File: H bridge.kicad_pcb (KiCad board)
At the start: 2 copper layers, 97 x 50 mm, 52 parts, among them J1 Fan, J2 5v Output, J3 Motor Terminal, J4 24v Power Input, J5 Control, J6 5v Output, J7 ICSP, Q1 IRLZ44N, Q2 IRLZ44N, Q3 IRLZ44N, Q4 IRLZ44N, SW1 SW_SPST, U1 IR2110, U2 IR2110, U3 LM7815_TO220, U4 ATmega328P-A, U5 LM7805_TO220, Y1 16MHz

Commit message: just made some modification for the final revision.. I might manufacture this one.
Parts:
- U3: value LM7815_TO220 -> LM7815
- U5: value LM7805_TO220 -> LM7805
- renumbered SW1 to OFF/ON

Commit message: small edit in pcb for fabrication.
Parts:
- added REF**: WEEE-Logo_5.6x8mm_SilkScreen, Symbol:WEEE-Logo_5.6x8mm_SilkScreen, B.Cu at (143.0, 104.5)
- added REF**: KiCad-Logo2_6mm_SilkScreen, Symbol:KiCad-Logo2_6mm_SilkScreen, B.Cu at (180.0, 91.0)
- added REF**: OSHW-Logo_7.5x8mm_SilkScreen, Symbol:OSHW-Logo_7.5x8mm_SilkScreen, B.Cu at (150.5, 104.5)
- moved G*** 0.79 mm to (174.0, 96.0)
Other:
- board text added: "v2.1"
- board text removed: "v2.0"

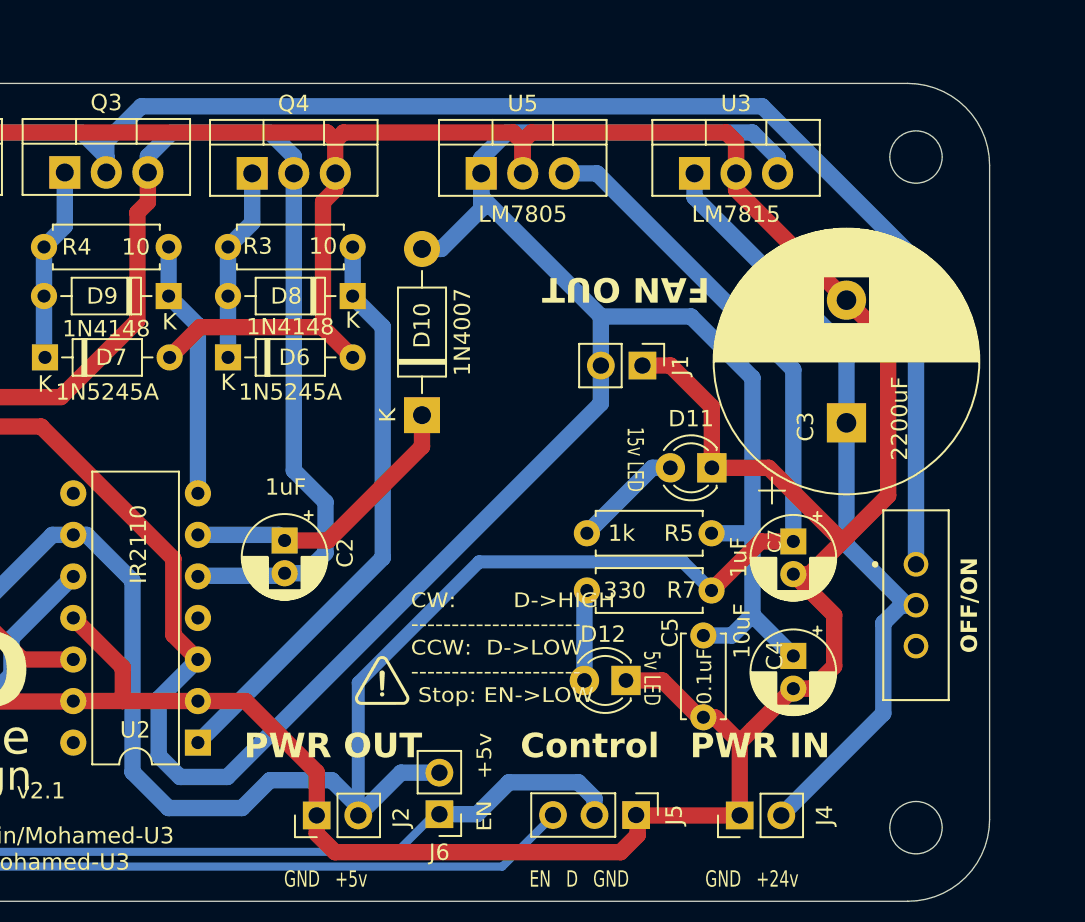
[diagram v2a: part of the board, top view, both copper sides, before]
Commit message: Feat: New SW for the Power + small changes.
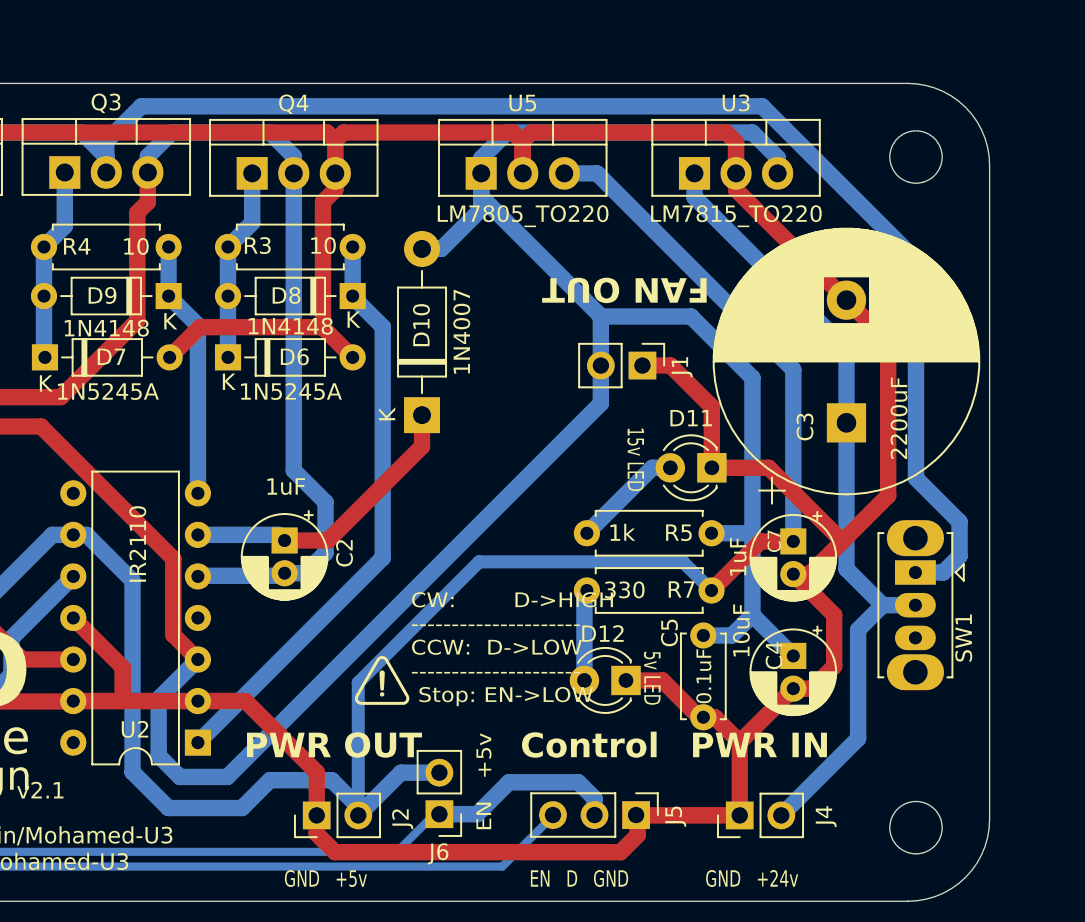
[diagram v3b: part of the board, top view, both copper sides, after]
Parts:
- removed OFF/ON: SW_SPST, Button_Switch_THT:SW_EG1218
- removed REF**: WEEE-Logo_5.6x8mm_SilkScreen, Symbol:WEEE-Logo_5.6x8mm_SilkScreen
- removed REF**: KiCad-Logo2_6mm_SilkScreen, Symbol:KiCad-Logo2_6mm_SilkScreen
- removed REF**: OSHW-Logo_7.5x8mm_SilkScreen, Symbol:OSHW-Logo_7.5x8mm_SilkScreen
- added SW1: SW_SPST, Button_Switch_THT:SW_Slide_SPDT_Straight_CK_OS102011MS2Q, F.Cu at (206.6, 89.4)
- U3: value LM7815 -> LM7815_TO220
- U5: value LM7805 -> LM7805_TO220
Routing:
- net Net-(Q1-D): track 101.7 -> 105.4 mm

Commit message: fix: small modifications on the PCB for perfection =D.
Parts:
- moved C6 0.34 mm to (125.7, 103.3)
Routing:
- net 13/SCK: track 14.8 -> 13.2 mm

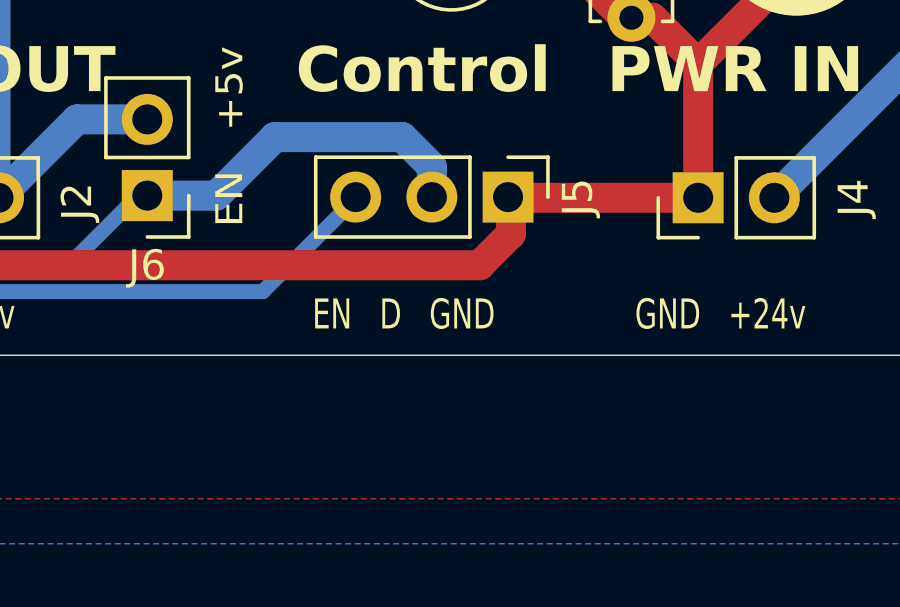
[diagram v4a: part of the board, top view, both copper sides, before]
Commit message: fix: small change in silkscreen cuz the EN and D was swaped :P
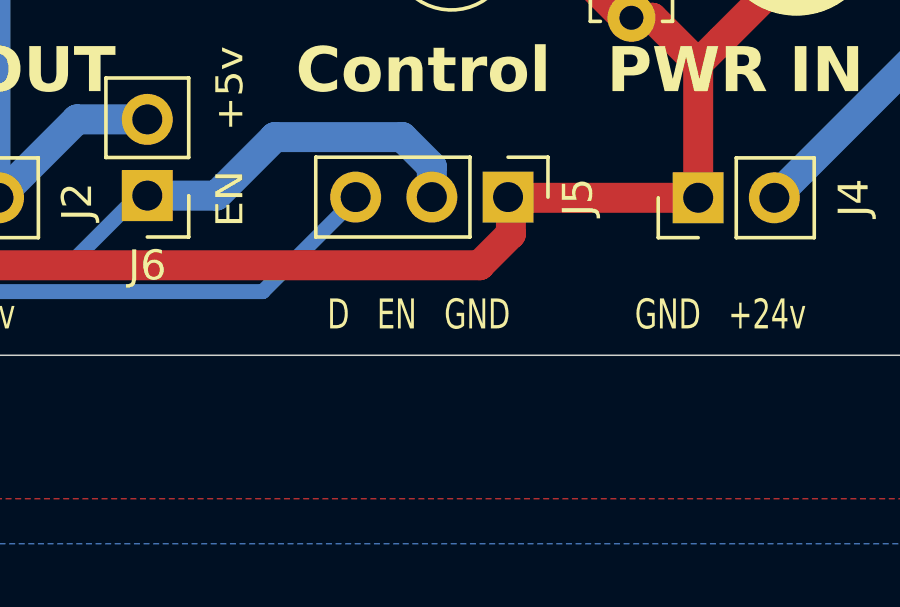
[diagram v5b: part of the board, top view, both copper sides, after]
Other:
- board text added: "D EN GND"
- board text removed: "EN D GND"
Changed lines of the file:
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@@
 		)
 	)
-	(gr_text "EN   D   GND"
-		(at 183 108.75 0)
+	(gr_text "D   EN   GND"
+		(at 183.5 108.75 0)
 		(layer "F.SilkS")
 		(effects
